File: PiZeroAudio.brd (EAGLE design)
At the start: 65.1 x 30.2 mm, 66 parts, among them CON1 RPI-ZERO, J1 GROVE, J2 2X2HEADER, J3 2X1-LOCKING, J4 4X1-LOCKING, Q1 DMG2305UX, U1 TXB0104PWR, U2 LSM6DS33, U3 NC7WZ16, U4 DMMT5401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

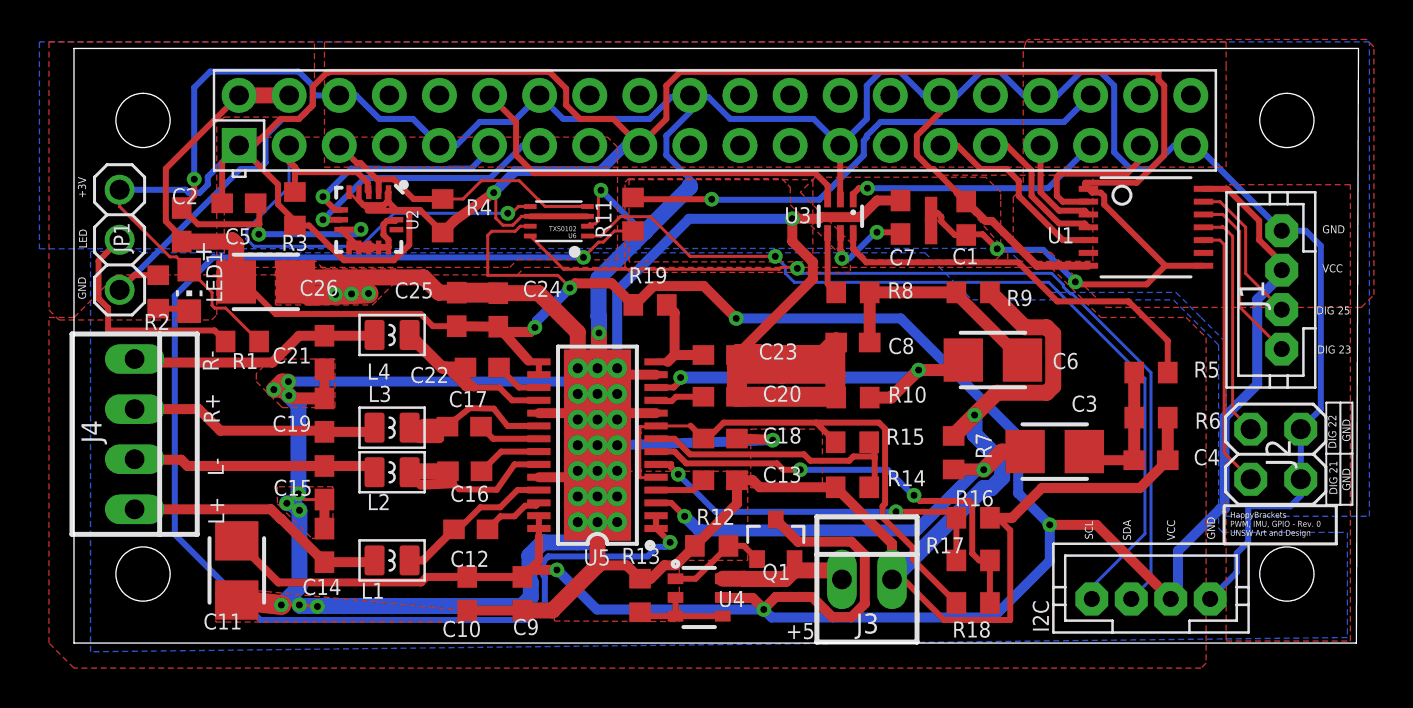
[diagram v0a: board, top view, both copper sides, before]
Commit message: Changed capacitor footprints
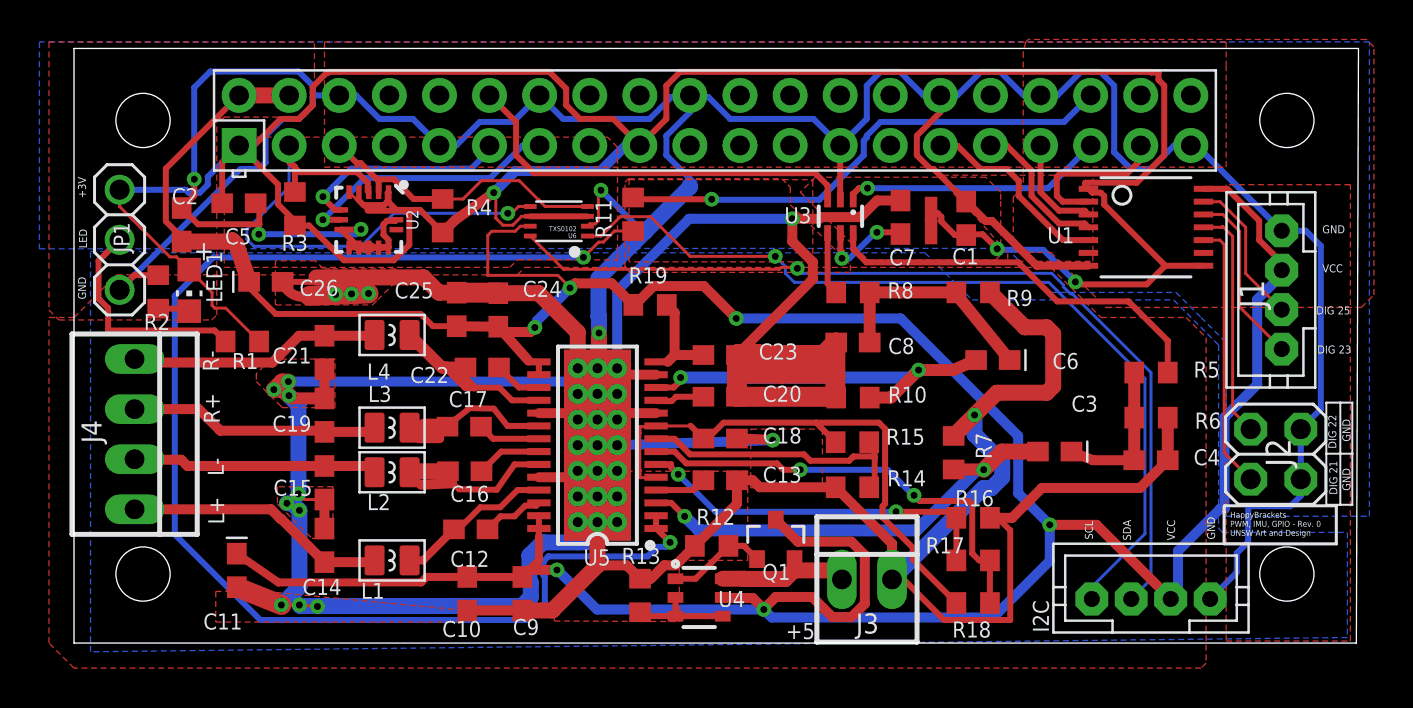
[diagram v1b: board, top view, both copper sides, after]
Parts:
- C1, C10, C2, C25, C4, C5, C7, C8: value 100nF -> 0.1uF
- C11, C3, C6: device adafruit:CT3528 -> HappyBrackets:0603-POLAR
- C26: value 100UF -> 100uF; device adafruit:CT3528 -> HappyBrackets:0603-POLAR
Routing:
- net AGND: track 305.8 -> 307.7 mm
- net AUDIO-LEFT: track 22.5 -> 23.1 mm
- net N$1: track 7.16 -> 7.71 mm
- net AUDIO-RIGHT: track 19.3 -> 19.8 mm

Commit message: Changed Capacitor sizes for tant caps
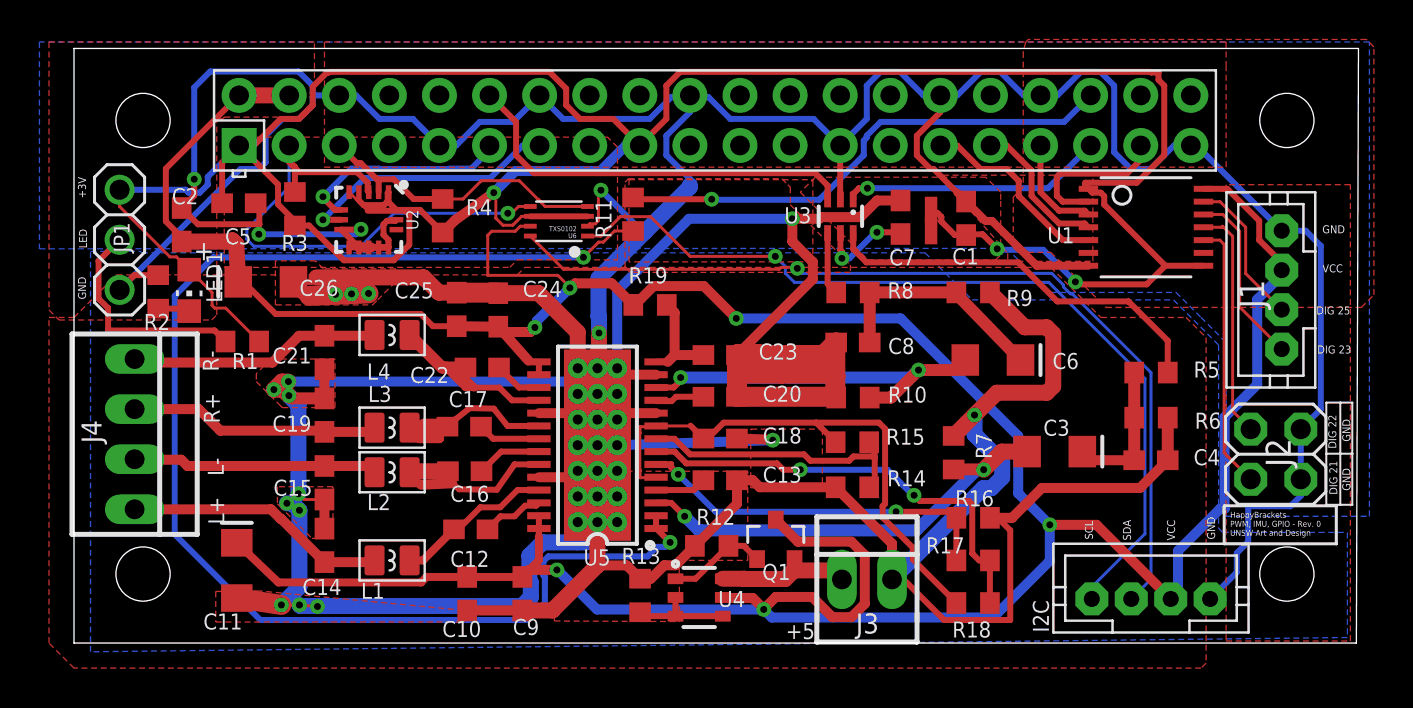
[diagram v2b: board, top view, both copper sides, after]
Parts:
- C11, C26, C3, C6: device HappyBrackets:0603-POLAR -> HappyBrackets:EIA3216
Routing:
- net AGND: track 307.7 -> 306.0 mm
- net AUDIO-LEFT: track 23.1 -> 22.6 mm
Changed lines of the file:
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@@
 <attribute name="SPICEPREFIX" value="C" x="-39.243" y="16.51" size="1.778" layer="27" rot="R180" display="off"/>
 </element>
-<element name="C3" library="HappyBrackets" library_urn="urn:adsk.eagle:library:5224691" package="0603-POLAR" value="47uF" x="-29.011625" y="10.978134375" smashed="yes">
-<attribute name="NAME" x="-26.827734375" y="13.812775" size="0.8128" layer="25" rot="R180"/>
-</element>
-<element name="C6" library="HappyBrackets" library_urn="urn:adsk.eagle:library:5224691" package="0603-POLAR" value="47uF" x="-32.147" y="15.621" smashed="yes">
+<element name="C3" library="HappyBrackets" library_urn="urn:adsk.eagle:library:5224691" package="EIA3216" value="47uF" x="-29.011625" y="10.978134375" smashed="yes">
+<attribute name="NAME" x="-28.250134375" y="12.593575" size="0.8128" layer="25" rot="R180"/>
+</element>
+<element name="C6" library="HappyBrackets" library_urn="urn:adsk.eagle:library:5224691" package="EIA3216" value="47uF" x="-32.147" y="15.621" smashed="yes">
 <attribute name="NAME" x="-29.1244" y="15.1638" size="0.8128" layer="25"/>
 </element>
@@
 <attribute name="SPICEPREFIX" value="C" x="-58.801" y="3.7721" size="1.778" layer="27" rot="R270" display="off"/>
 </element>
-<element name="C11" library="HappyBrackets" library_urn="urn:adsk.eagle:library:5224691" package="0603-POLAR" value="100uF" x="-70.485" y="4.953" smashed="yes" rot="R90">
+<element name="C11" library="HappyBrackets" library_urn="urn:adsk.eagle:library:5224691" package="EIA3216" value="100uF" x="-70.485" y="4.953" smashed="yes" rot="R90">
 <attribute name="NAME" x="-70.2056" y="2.7686" size="0.8128" layer="25" rot="R180"/>
 </element>
@@
 <attribute name="SPICEPREFIX" value="C" x="-59.3344" y="18.1864" size="1.778" layer="27" rot="R90" display="off"/>
 </element>
-<element name="C26" library="HappyBrackets" library_urn="urn:adsk.eagle:library:5224691" package="0603-POLAR" value="100uF" x="-69.0118" y="19.5834" smashed="yes" rot="R180">
+<element name="C26" library="HappyBrackets" library_urn="urn:adsk.eagle:library:5224691" package="EIA3216" value="100uF" x="-69.0118" y="19.5834" smashed="yes" rot="R180">
 <attribute name="NAME" x="-65.3288" y="19.685" size="0.8128" layer="25" rot="R180"/>
 </element>
@@
 <contactref element="U4" pad="E2"/>
 <contactref element="J1" pad="3"/>
-<wire x1="-69.8618" y1="19.5834" x2="-70.14445" y2="19.5834" width="0.3048" layer="1"/>
+<wire x1="-70.4118" y1="19.5834" x2="-70.14445" y2="19.5834" width="0.3048" layer="1"/>
 <wire x1="-60.54074375" y1="17.3364" x2="-59.3344" y2="17.3364" width="0.3048" layer="1"/>
 <wire x1="-61.16214375" y1="17.9578" x2="-60.54074375" y2="17.3364" width="0.3048" layer="1"/>
@@
 <wire x1="-60.8624" y1="4.6221" x2="-58.801" y2="4.6221" width="0.4064" layer="1"/>
 <wire x1="-68.3754" y1="4.3434" x2="-61.1411" y2="4.3434" width="0.4064" layer="1"/>
-<wire x1="-70.485" y1="5.803" x2="-68.3754" y2="4.3434" width="0.4064" layer="1"/>
+<wire x1="-70.485" y1="6.353" x2="-68.3754" y2="4.3434" width="0.4064" layer="1"/>
 <wire x1="-58.801" y1="4.6221" x2="-56.007" y2="4.6221" width="0.4064" layer="1"/>
 <wire x1="-56.007" y1="4.6221" x2="-55.66375" y2="4.96535" width="0.4064" layer="1"/>
@@
 <wire x1="-54.2036" y1="19.9136" x2="-53.5686" y2="19.2786" width="0.1524" layer="1"/>
 <wire x1="-57.5536" y1="22.1516" x2="-57.7596" y2="21.9456" width="0.1524" layer="1"/>
-<wire x1="-69.8618" y1="19.5834" x2="-70.5118" y2="21.4898" width="0.8128" layer="1"/>
+<wire x1="-70.4118" y1="19.5834" x2="-70.5118" y2="21.4898" width="0.8128" layer="1"/>
 <wire x1="-70.5118" y1="21.4898" x2="-70.7136" y2="21.6916" width="0.8128" layer="1"/>
 <wire x1="-70.7136" y1="21.6916" x2="-70.7762" y2="21.629" width="0.8128" layer="1"/>
@@
 <wire x1="-24.98" y1="12.7" x2="-24.98" y2="14.986" width="0.6096" layer="1"/>
 <wire x1="-24.98" y1="10.541" x2="-27.074490625" y2="10.541" width="0.508" layer="1"/>
-<wire x1="-27.074490625" y1="10.541" x2="-28.161625" y2="10.978134375" width="0.508" layer="1"/>
+<wire x1="-27.074490625" y1="10.541" x2="-27.611625" y2="10.978134375" width="0.508" layer="1"/>
 </signal>
 <signal name="N$4">
@@
 <wire x1="-34.3154" y1="19.05" x2="-38.393" y2="19.05" width="0.6096" layer="1"/>
 <wire x1="-38.393" y1="19.05" x2="-38.393" y2="16.51" width="0.6096" layer="1"/>
-<wire x1="-31.297" y1="15.621" x2="-34.076" y2="19.05" width="0.6096" layer="1"/>
+<wire x1="-30.747" y1="15.621" x2="-34.076" y2="19.05" width="0.6096" layer="1"/>
 <wire x1="-34.076" y1="19.05" x2="-34.3154" y2="19.05" width="0.6096" layer="1"/>
 </signal>
@@
 <contactref element="C8" pad="2"/>
 <contactref element="R10" pad="1"/>
-<wire x1="-66.804775" y1="18.8762" x2="-68.1618" y2="19.5834" width="0.508" layer="1" curve="-90"/>
+<wire x1="-66.804775" y1="18.8762" x2="-67.6118" y2="19.5834" width="0.508" layer="1" curve="-90"/>
 <wire x1="-57.2516" y1="19.0364" x2="-57.2262" y2="19.011" width="0.508" layer="1"/>
 <contactref element="U5" pad="GND@10"/>
@@
 <wire x1="-63.8302" y1="18.9738" x2="-63.8048" y2="18.9992" width="0.3048" layer="1"/>
 <wire x1="-52.197" y1="11.303" x2="-52.197" y2="14.6812" width="0.3048" layer="1"/>
-<wire x1="-68.1618" y1="19.5834" x2="-66.675" y2="19.5834" width="0.3048" layer="1"/>
+<wire x1="-67.6118" y1="19.5834" x2="-66.675" y2="19.5834" width="0.3048" layer="1"/>
 <wire x1="-52.197" y1="11.303" x2="-50.5974" y2="12.9026" width="0.1524" layer="1"/>
 <wire x1="-50.5974" y1="12.9026" x2="-50.5974" y2="12.928" width="0.1524" layer="1"/>
-<wire x1="-68.1618" y1="19.5834" x2="-66.675" y2="19.5834" width="0.1524" layer="1"/>
+<wire x1="-67.6118" y1="19.5834" x2="-66.675" y2="19.5834" width="0.1524" layer="1"/>
 <wire x1="-66.675" y1="19.5834" x2="-66.4464" y2="19.812" width="0.1524" layer="1"/>
 <wire x1="-59.3344" y1="19.0364" x2="-57.2516" y2="19.0364" width="1.016" layer="1"/>
@@
 <vertex x="-41.275" y="24.7396"/>
 </polygon>
-<wire x1="-68.2244" y1="3.2004" x2="-70.485" y2="4.103" width="1.016" layer="1"/>
+<wire x1="-68.2244" y1="3.2004" x2="-70.485" y2="3.553" width="1.016" layer="1"/>
 <wire x1="-42.3164" y1="22.7838" x2="-47.5488" y2="22.7838" width="0.508" layer="16"/>
 <wire x1="-42.3164" y1="21.63279375" x2="-41.2778" y2="20.59419375" width="0.508" layer="1"/>
@@
 <wire x1="-36.0172" y1="6.985" x2="-32.9692" y2="10.033" width="0.6096" layer="16"/>
 <wire x1="-32.6136" y1="10.0584" x2="-31.693865625" y2="10.978134375" width="0.8128" layer="1"/>
-<wire x1="-31.693865625" y1="10.978134375" x2="-29.861625" y2="10.978134375" width="0.8128" layer="1"/>
+<wire x1="-31.693865625" y1="10.978134375" x2="-30.411625" y2="10.978134375" width="0.8128" layer="1"/>
 </signal>
 <signal name="AUDIO-RIGHT">
@@
 <via x="-35.9156" y="15.113" extent="1-16" drill="0.35"/>
 <wire x1="-35.9156" y1="15.113" x2="-34.155" y2="15.113" width="0.6096" layer="1"/>
-<wire x1="-34.155" y1="15.113" x2="-32.997" y2="15.621" width="0.6096" layer="1"/>
+<wire x1="-34.155" y1="15.113" x2="-33.547" y2="15.621" width="0.6096" layer="1"/>
 <wire x1="-35.9156" y1="15.113" x2="-37.3126" y2="13.716" width="0.6096" layer="1"/>
 <wire x1="-37.3126" y1="13.716" x2="-38.393" y2="13.716" width="0.6096" layer="1"/>
